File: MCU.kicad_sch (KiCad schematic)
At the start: 55 parts, among them J4 Conn_01x06_Pin, U1 STM32H723ZGT6, U51 24AA02-OT, Y5 12M, Y6 32,768kHz

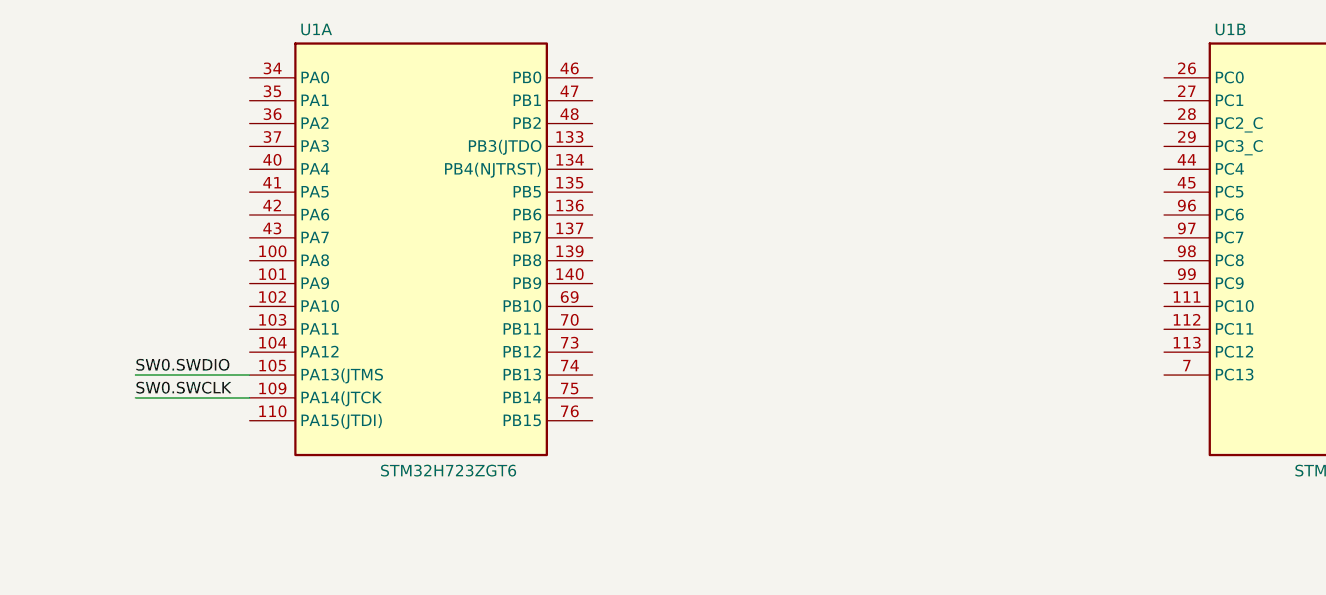
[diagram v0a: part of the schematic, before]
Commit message: wiring MCU to input and ouput
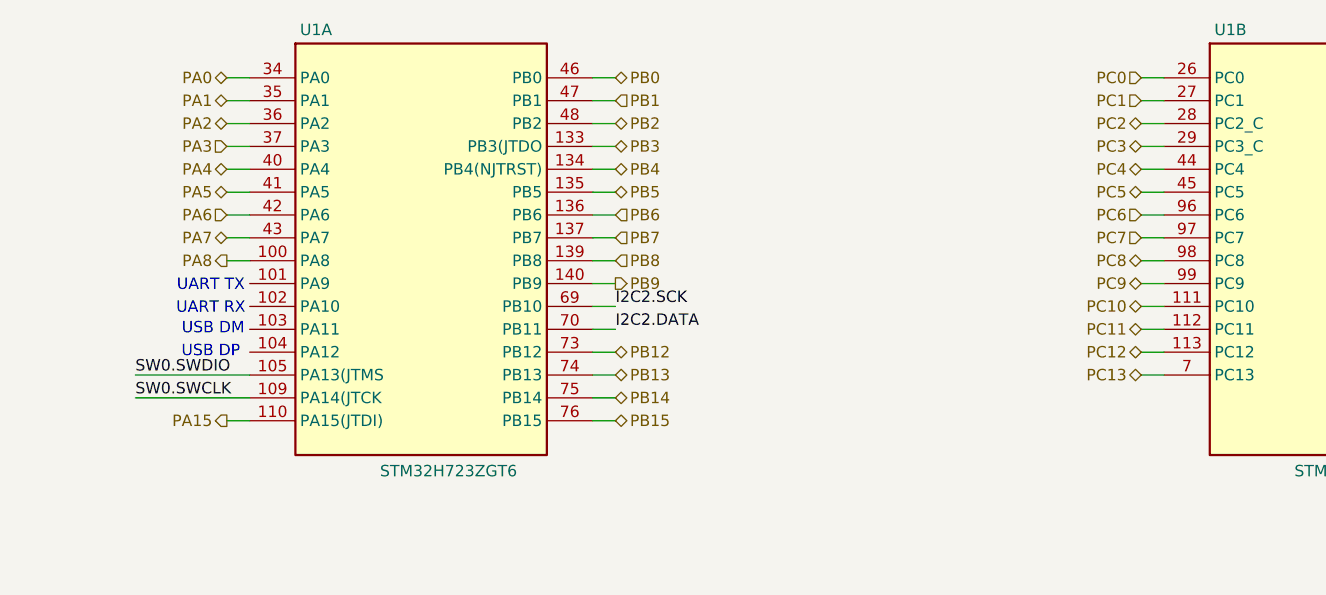
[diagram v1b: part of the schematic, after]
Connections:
- net I2C2.DATA: now also U1.70 (PB11)
- net I2C2.SCK: now also U1.69 (PB10)
- net PC10: now reaches U1.111 (PC10)
- net PC11: now reaches U1.112 (PC11)
- net PC12: now reaches U1.113 (PC12)
- net PC0: now reaches U1.26 (PC0)
- net PC1: now reaches U1.27 (PC1)
- net PC2: now reaches U1.28 (PC2_C)
- net PC3: now reaches U1.29 (PC3_C)
- net PC4: now reaches U1.44 (PC4)
- net PC5: now reaches U1.45 (PC5)
- net PC13: now reaches U1.7 (PC13)
- net PC6: now reaches U1.96 (PC6)
- net PC7: now reaches U1.97 (PC7)
- net PC8: now reaches U1.98 (PC8)
- net PC9: now reaches U1.99 (PC9)
- net PA8: now reaches U1.100 (PA8)
- net PA15: now reaches U1.110 (PA15(JTDI))
- net PB3: now reaches U1.133 (PB3(JTDO)
- net PB4: now reaches U1.134 (PB4(NJTRST))
- net PB5: now reaches U1.135 (PB5)
- net PB6: now reaches U1.136 (PB6)
- net PB7: now reaches U1.137 (PB7)
- net PB8: now reaches U1.139 (PB8)
- net PB9: now reaches U1.140 (PB9)
- net PA0: now reaches U1.34 (PA0)
- net PA1: now reaches U1.35 (PA1)
- net PA2: now reaches U1.36 (PA2)
- net PA3: now reaches U1.37 (PA3)
- net PA4: now reaches U1.40 (PA4)
- net PA5: now reaches U1.41 (PA5)
- net PA6: now reaches U1.42 (PA6)
- net PA7: now reaches U1.43 (PA7)
- net PB0: now reaches U1.46 (PB0)
- net PB1: now reaches U1.47 (PB1)
- net PB2: now reaches U1.48 (PB2)
- net PB12: now reaches U1.73 (PB12)
- net PB13: now reaches U1.74 (PB13)
- net PB14: now reaches U1.75 (PB14)
- net PB15: now reaches U1.76 (PB15)
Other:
- note added: "UART RX"
- note added: "UART TX"
- note added: "USB DM"
- note added: "USB DP"

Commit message: started pin assignement
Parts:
- renumbered C284 to C20, C285 to C21, C282 to C22, C283 to C23, C321 to C24, C251 to C25, C292 to C26, C256 to C27, C257 to C28, C258 to C29, C261 to C30, C262 to C31, C263 to C32, C264 to C33, C269 to C34, C248 to C35, C265 to C36, C266 to C37, C270 to C38, C249 to C39, C267 to C40, C268 to C41, C247 to C42, C259 to C43, C260 to C44, C271 to C45, C250 to C46, J4 to J22, L24 to L4, R233 to R10, R226 to R11, R220 to R12, R227 to R13, R228 to R14, R263 to R15, R264 to R16, R216 to R17, R208 to R18, R217 to R19, R209 to R20, R211 to R21, R218 to R22, R210 to R23, R212 to R24, R219 to R25, R234 to R9, TP28 to TP1, TP12 to TP3, TP13 to TP4, TP14 to TP5, U51 to U2, Y6 to Y1, Y5 to Y2
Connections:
- net PD0: now reaches U1.114 (PD0)
- net PD1: now reaches U1.115 (PD1)
- net PD2: now reaches U1.116 (PD2)
- net PD3: now reaches U1.117 (PD3)
- net PD4: now reaches U1.118 (PD4)
- net PD5: now reaches U1.119 (PD5)
- net PD6: now reaches U1.122 (PD6)
- net PD7: now reaches U1.123 (PD7)
- net PD8: now reaches U1.77 (PD8)
- net PD9: now reaches U1.78 (PD9)
- net PD10: now reaches U1.79 (PD10)
- net PD11: now reaches U1.80 (PD11)
- net PD12: now reaches U1.81 (PD12)
- net PD13: now reaches U1.82 (PD13)
- net PD14: now reaches U1.85 (PD14)
- net PD15: now reaches U1.86 (PD15)
- net PG9: now reaches U1.124 (PG9)
- net PG10: now reaches U1.125 (PG10)
- net PG11: now reaches U1.126 (PG11)
- net PG12: now reaches U1.127 (PG12)
- net PG13: now reaches U1.128 (PG13)
- net PG14: now reaches U1.129 (PG14)
- net PG15: now reaches U1.132 (PG15)
- net PG0: now reaches U1.56 (PG0)
- net PG1: now reaches U1.57 (PG1)
- net PG2: now reaches U1.87 (PG2)
- net PG3: now reaches U1.88 (PG3)
- net PG4: now reaches U1.89 (PG4)
- net PG5: now reaches U1.90 (PG5)
- net PG6: now reaches U1.91 (PG6)
- net PG7: now reaches U1.92 (PG7)
- net PG8: now reaches U1.93 (PG8)
- net PE2: now reaches U1.1 (PE2)
- net PF0: now reaches U1.10 (PF0)
- net PF1: now reaches U1.11 (PF1)
- net PF2: now reaches U1.12 (PF2)
- net PF3: now reaches U1.13 (PF3)
- net PF4: now reaches U1.14 (PF4)
- net PE0: now reaches U1.141 (PE0)
- net PE1: now reaches U1.142 (PE1)
- net PF5: now reaches U1.15 (PF5)
- net PF6: now reaches U1.18 (PF6)
- net PF7: now reaches U1.19 (PF7)
- net PF8: now reaches U1.20 (PF8)
- net PF9: now reaches U1.21 (PF9)
- net PF10: now reaches U1.22 (PF10)
- net PF11: now reaches U1.49 (PF11)
- net PF12: now reaches U1.50 (PF12)
- net PF13: now reaches U1.53 (PF13)
- net PF14: now reaches U1.54 (PF14)
- net PF15: now reaches U1.55 (PF15)
- no-connect marks 0 -> 2
